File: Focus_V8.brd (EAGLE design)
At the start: 64.8 x 94 mm, 104 parts, among them X1 USB+SHIELD

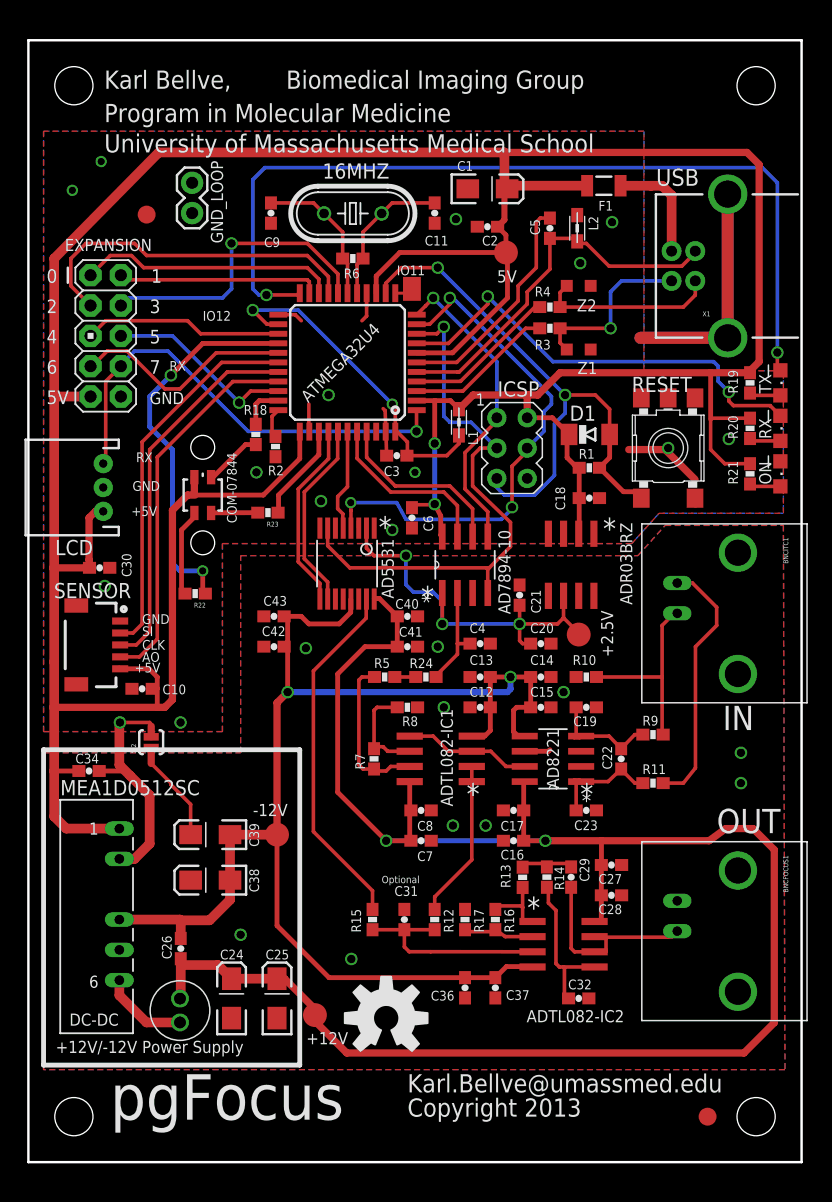
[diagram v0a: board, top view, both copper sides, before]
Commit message: Changed connector for Expansion, cleaned up text
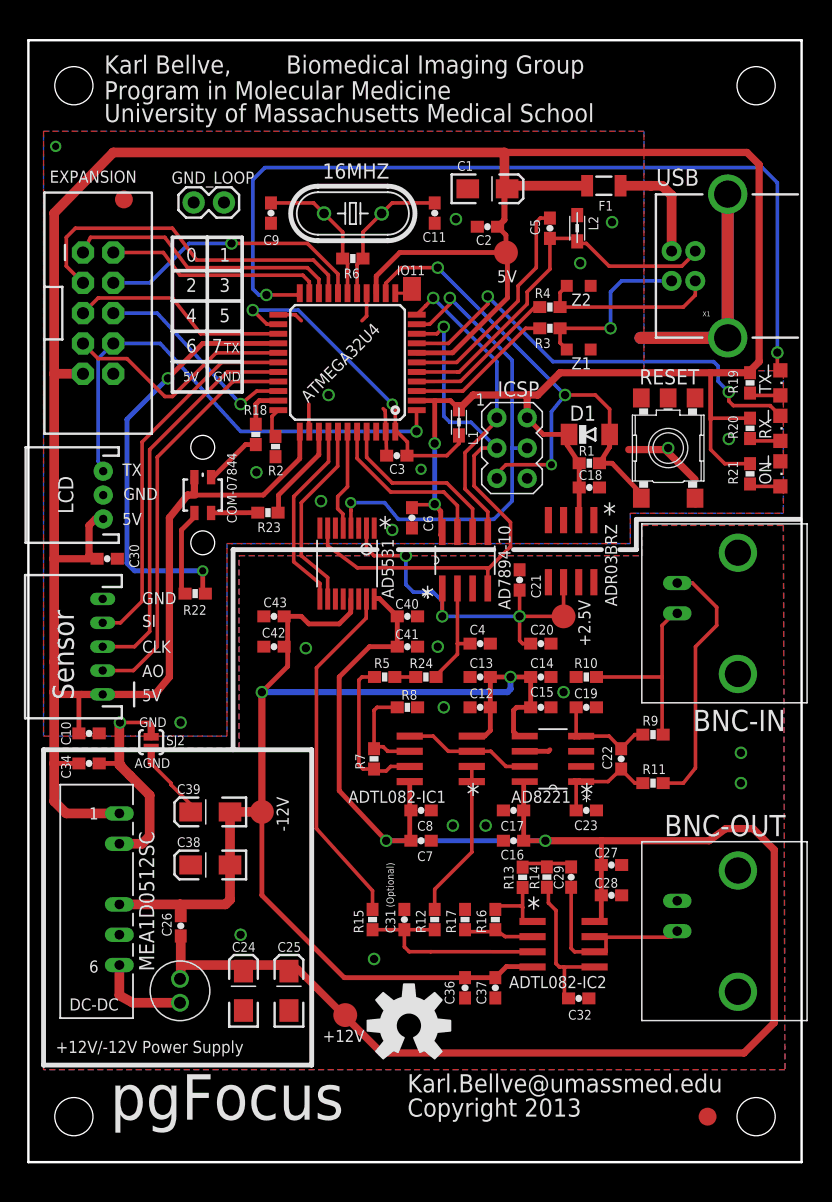
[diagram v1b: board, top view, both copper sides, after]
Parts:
- C1: value 10uF -> 10uF (16V)
- C10, C18, C3, C34, C5: value 1uF -> 1uF (16V)
- C11, C9: value 18pF -> 18pF (16V)
- C12, C15, C17, C20, C28, C31, C37, C4, C40, C43, C8: value 0.1uF -> 0.1uF (50V)
- C16, C26, C27, C36, C41, C42, C7: value 1uF -> 1uF (50V)
- C19, C23, C29, C32: value 1000pF -> 1000pF (50V)
- C2: value 0.1uF -> 0.1uF (16V)
- C22: value 0.01uF -> 0.01uF (50V)
- C24, C25, C38, C39: value 10uF -> 10uF (35V)
- EXPANSION: value M05X2PTH -> M05X2SHD; device SparkFun:AVR_ICSP -> SparkFun-Connectors:2X5-SHROUDED
- SENSOR: value PRT-10209 -> M05; device SparkFun-Connectors:1X05-1MM-RA -> BIG:M05JST-PTH
- moved C10 5.81 mm to (40.6, 34.6), turned to 0 degrees
- moved +12V 2.54 mm to (62.1, 11.0)
- moved -12V 2.29 mm to (55.1, 28.1)
- moved JP2 2.29 mm to (43.6, 79.4)
- moved U$3 2.01 mm to (67.4, 10.2)
- moved EXPANSION 2.01 mm to (41.4, 69.8)
- moved +2.5V 1.98 mm to (80.4, 44.5)
- moved C26 1.91 mm to (48.3, 18.5)
- moved C39 1.91 mm to (50.8, 28.1)
- moved GND_LOOP 1.66 mm to (49.4, 79.1), turned to 0 degrees
- moved L3 1.65 mm to (48.3, 13.1)
- moved SENSOR 1.47 mm to (41.8, 41.9), turned to 0 degrees
- moved C38 1.27 mm to (50.8, 23.6)
- moved MEA1D0512SC 1.27 mm to (43.2, 21.6)
- moved C21 1.27 mm to (76.7, 47.5)
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- renumbered BNCFOCUS1 to BNC-OUT, BNCITC1 to BNC-IN
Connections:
- net +5V: now also SENSOR.P$1; no longer SENSOR.5
- net GND: now also SENSOR.P$5; no longer SENSOR.1
- net TSL1401R_AO: now also SENSOR.P$2; no longer SENSOR.4
- net TSL1401R_CLK: now also SENSOR.P$3; no longer SENSOR.3
- net TSL1401R_SI: now also SENSOR.P$4; no longer SENSOR.2
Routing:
- net +5V: track 314.8 -> 307.8 mm
- net IO12: track 32.1 -> 35.9 mm
- net D7: track 38.7 -> 41.8 mm
- net D3/SCL: track 25.2 -> 22.9 mm
- net TSL1401R_AO: track 31.7 -> 34.0 mm
- net RESET: track 49.1 -> 46.8 mm, vias 2 -> 3
- net MOSI: track 43.5 -> 41.4 mm, vias 3 -> 2
- net -12V: track 115.6 -> 117.6 mm
- net AGND: track 10.8 -> 8.92 mm
- net D5: track 15.9 -> 17.6 mm
- net D4: track 16.8 -> 18.4 mm
- net D1/TX: track 17.0 -> 18.6 mm
- net D0/RX: track 21.8 -> 23.4 mm
- net TSL1401R_CLK: track 31.6 -> 33.2 mm
- net +12V: track 154.0 -> 155.4 mm
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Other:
- board text added: "(Optional)"
- board text added: "AGND"
- board text added: "Sensor"
- board text added: "TX"
- board text removed: "+5V"
- board text removed: "IN"
- board text removed: "IO12"
- board text removed: "OUT"
- board text removed: "Optional"
- board text removed: "RX"

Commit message: Switchedd top two holes 1/8" Vias for mounting for chasis grounding
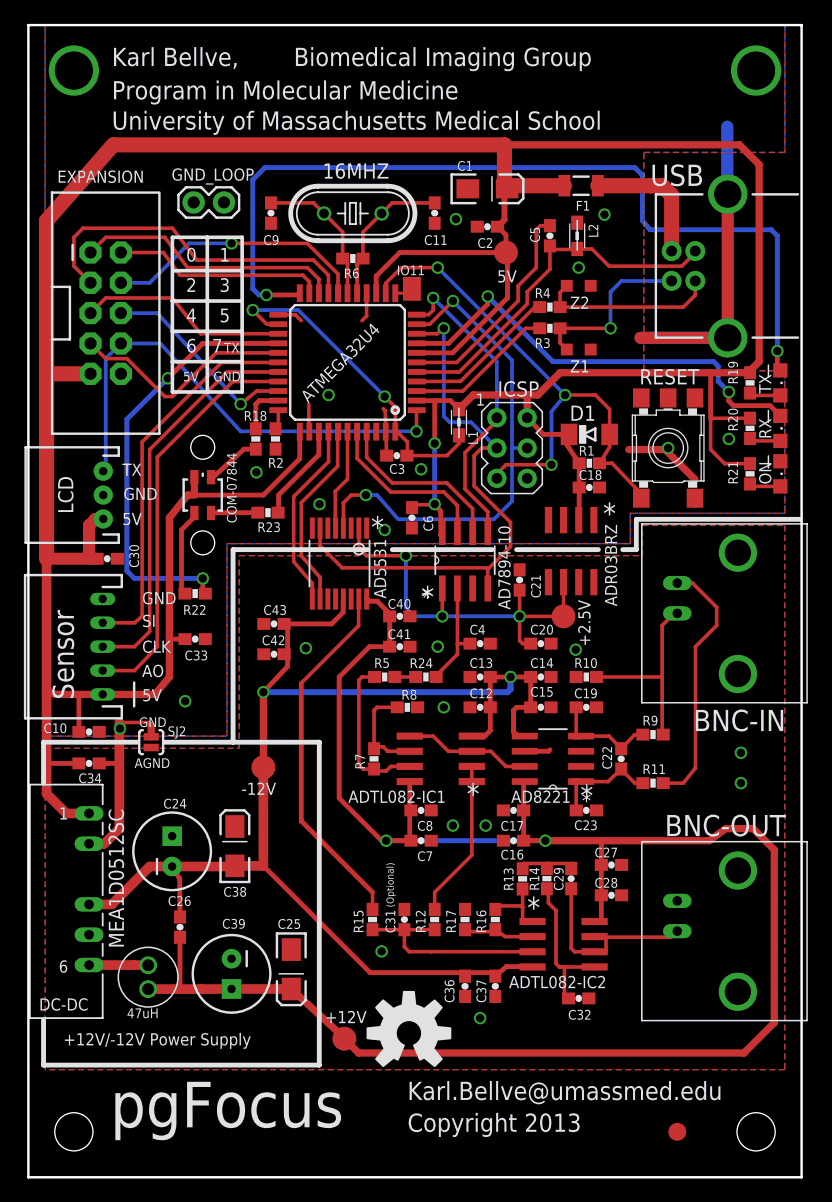
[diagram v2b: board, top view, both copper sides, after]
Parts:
- removed JP2: FIDUCIAL1.5X3, SparkFun:FIDUCIAL-1.5X3
- added C33: 1uF (16V), SparkFun:0603-CAP
- C24, C39: value 10uF (35V) -> 10uF (PLF1E100MCL7TP); device SparkFun:EIA3216-KIT -> SparkFun-Passives:CPOL-RADIAL-100UF-25V
- moved C39 13.7 mm to (52.6, 14.5), turned to 270 degrees
- moved C24 13.1 mm to (47.6, 24.8)
- moved -12V 3.74 mm to (55.2, 31.8)
- moved L3 2.90 mm to (45.6, 14.2), turned to 270 degrees
- moved JP1 2.84 mm to (89.9, 1.27)
- moved C38 2.59 mm to (52.9, 25.2), turned to 90 degrees
- moved MEA1D0512SC 2.54 mm to (40.6, 21.6)
- moved +12V 1.98 mm to (62.0, 9.07)
- moved F1 1.91 mm to (81.9, 80.5)
- moved C25 1.81 mm to (57.6, 14.9), turned to 270 degrees
- moved C40 0.64 mm to (66.7, 44.5)
- moved C41 0.64 mm to (66.7, 41.9)
- moved C43 0.64 mm to (56.1, 43.8)
- moved C5 0.64 mm to (79.2, 76.3)
- moved L2 0.64 mm to (81.5, 76.3)
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- renumbered X1 to USB
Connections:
- net +12V: now also C39.1; no longer C24.A
- net +5V: now also C33.2
- net -12V: now also C24.2; no longer C39.C
- net AGND: now also C24.1, C39.2; no longer C24.C, C39.A
- net GND: now also C33.1
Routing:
- net GND: track 78.0 -> 68.8 mm, vias 13 -> 14
- net AGND: track 8.92 -> 2.16 mm
- net -12V: track 117.6 -> 114.7 mm
- net N$6: track 7.78 -> 4.95 mm
- net N$22: track 9.28 -> 11.2 mm
- net +12V: track 155.4 -> 156.5 mm
- net 2.5V_REFIN: track 33.3 -> 34.3 mm
- net N$8: track 29.5 -> 30.5 mm
- net D0/RX: track 23.4 -> 22.5 mm
- net HWB: track 2.50 -> 1.66 mm
- net TSL1401R_SI: track 31.6 -> 32.3 mm
- net D7: track 41.8 -> 41.1 mm
- net D5: track 17.6 -> 16.9 mm
- net D4: track 18.4 -> 17.8 mm
- net D3/SCL: track 22.9 -> 22.2 mm
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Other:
- board size 64.8 x 94 mm -> 64.8 x 96.5 mm
- board text added: "47uH"
- board text removed: "USB"
